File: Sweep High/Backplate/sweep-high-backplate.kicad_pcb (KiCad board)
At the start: 2 copper layers, 229.5 x 95.2 mm, 13 parts

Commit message: added logo on backplate
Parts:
- added G***: LOGO, Kailh:ferris_broom, B.Cu at (82.0, 118.1)

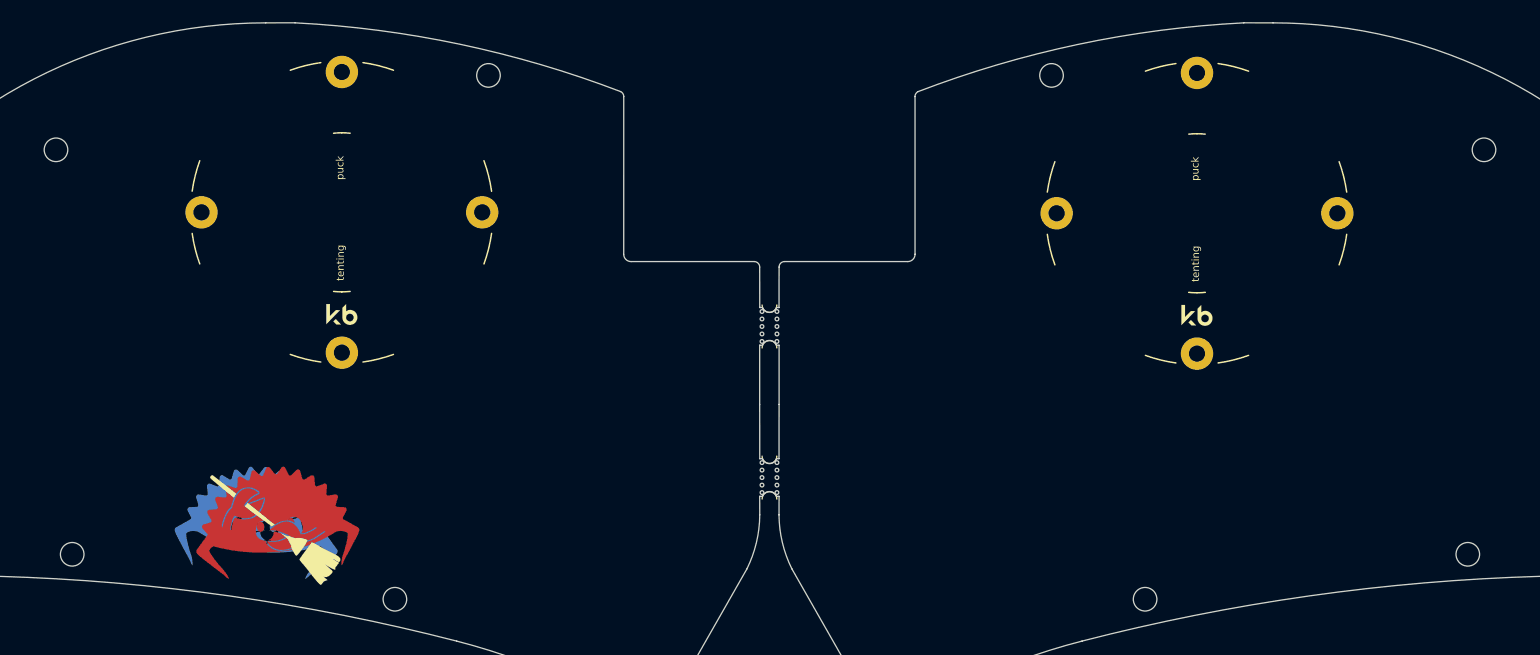
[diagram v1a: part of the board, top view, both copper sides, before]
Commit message: somehow some more things I missed, namely mount hole sizes
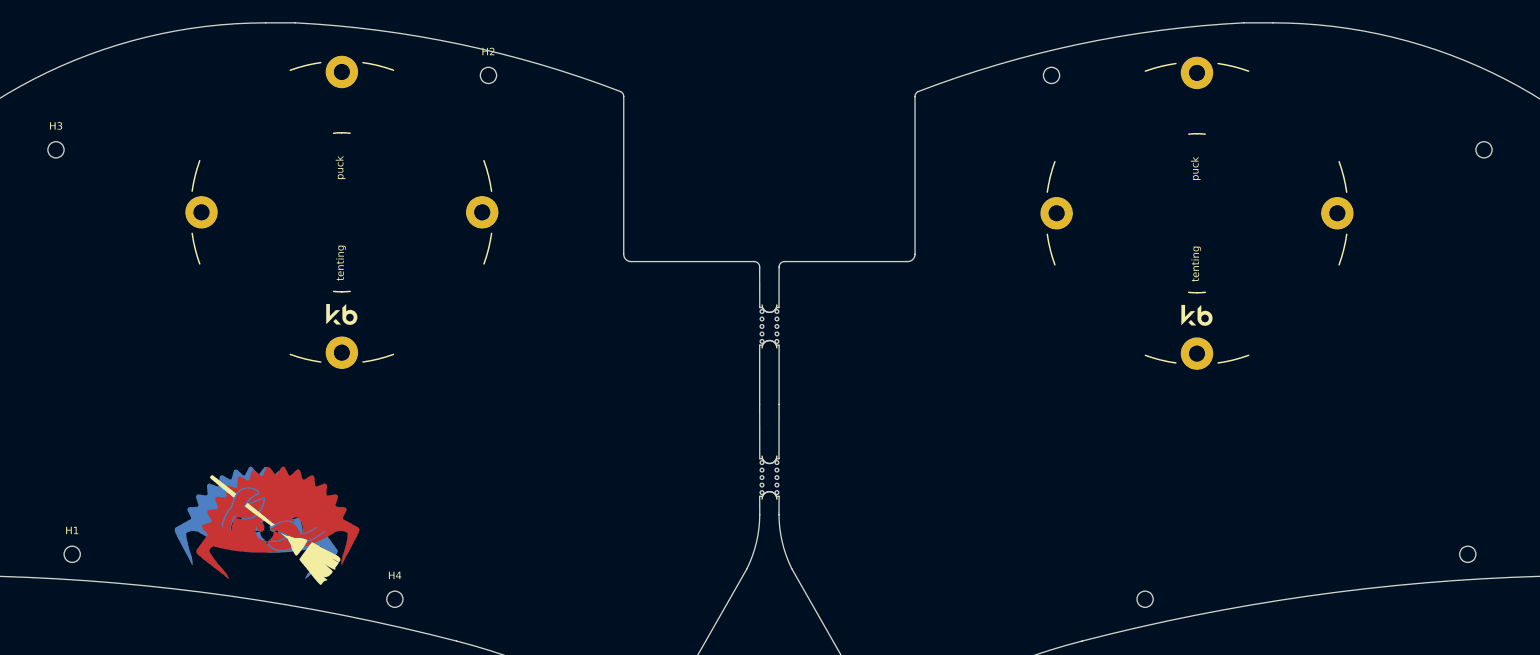
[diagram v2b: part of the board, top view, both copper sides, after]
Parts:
- H1, H2, H3, H4, H5, H6, H7, H8: footprint MountingHole:MountingHole_3.2mm_M3 -> MountingHole:MountingHole_2.2mm_M2
